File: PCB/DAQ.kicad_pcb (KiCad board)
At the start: 2 copper layers, 164 x 140 mm, 58 parts, among them IC1 MAX743CWE+, J1 Arduino_Mega_Header, J10 Conn_01x01, J11 Conn_01x01, J12 Conn_01x01, J2 Conn_01x07, J3 Conn_01x08, J4 Conn_01x08, J5 Conn_02x18_Counter_Clockwise, J6 Conn_01x10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

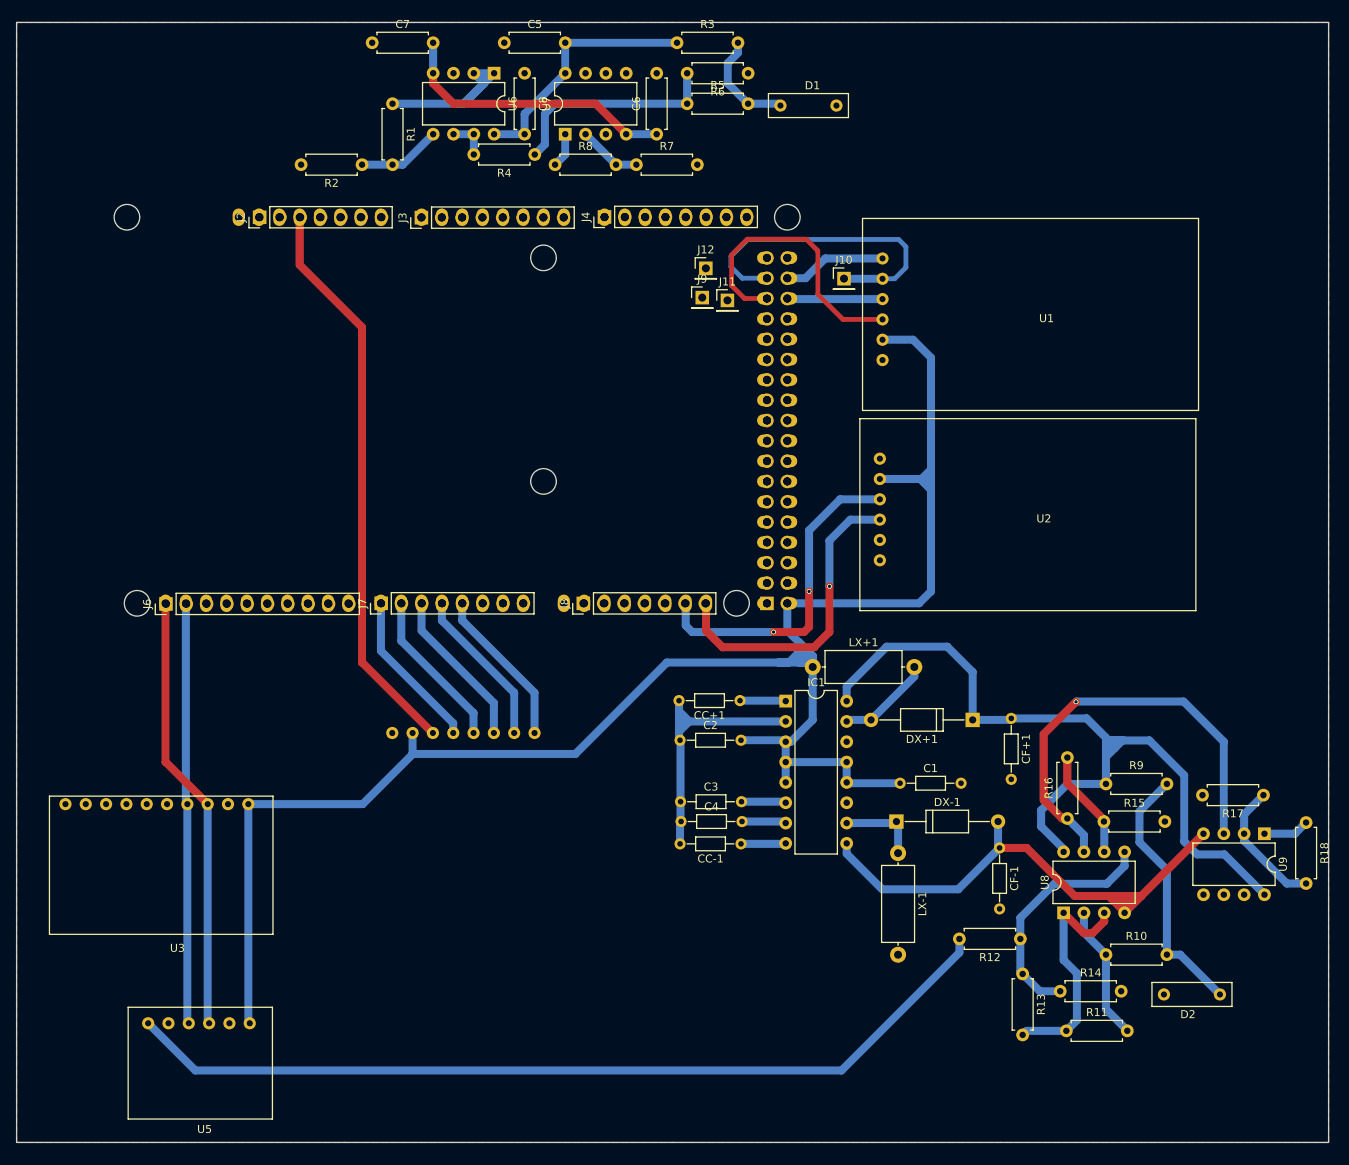
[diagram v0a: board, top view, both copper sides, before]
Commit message: PCB Upgraded and screens of the DAC analog
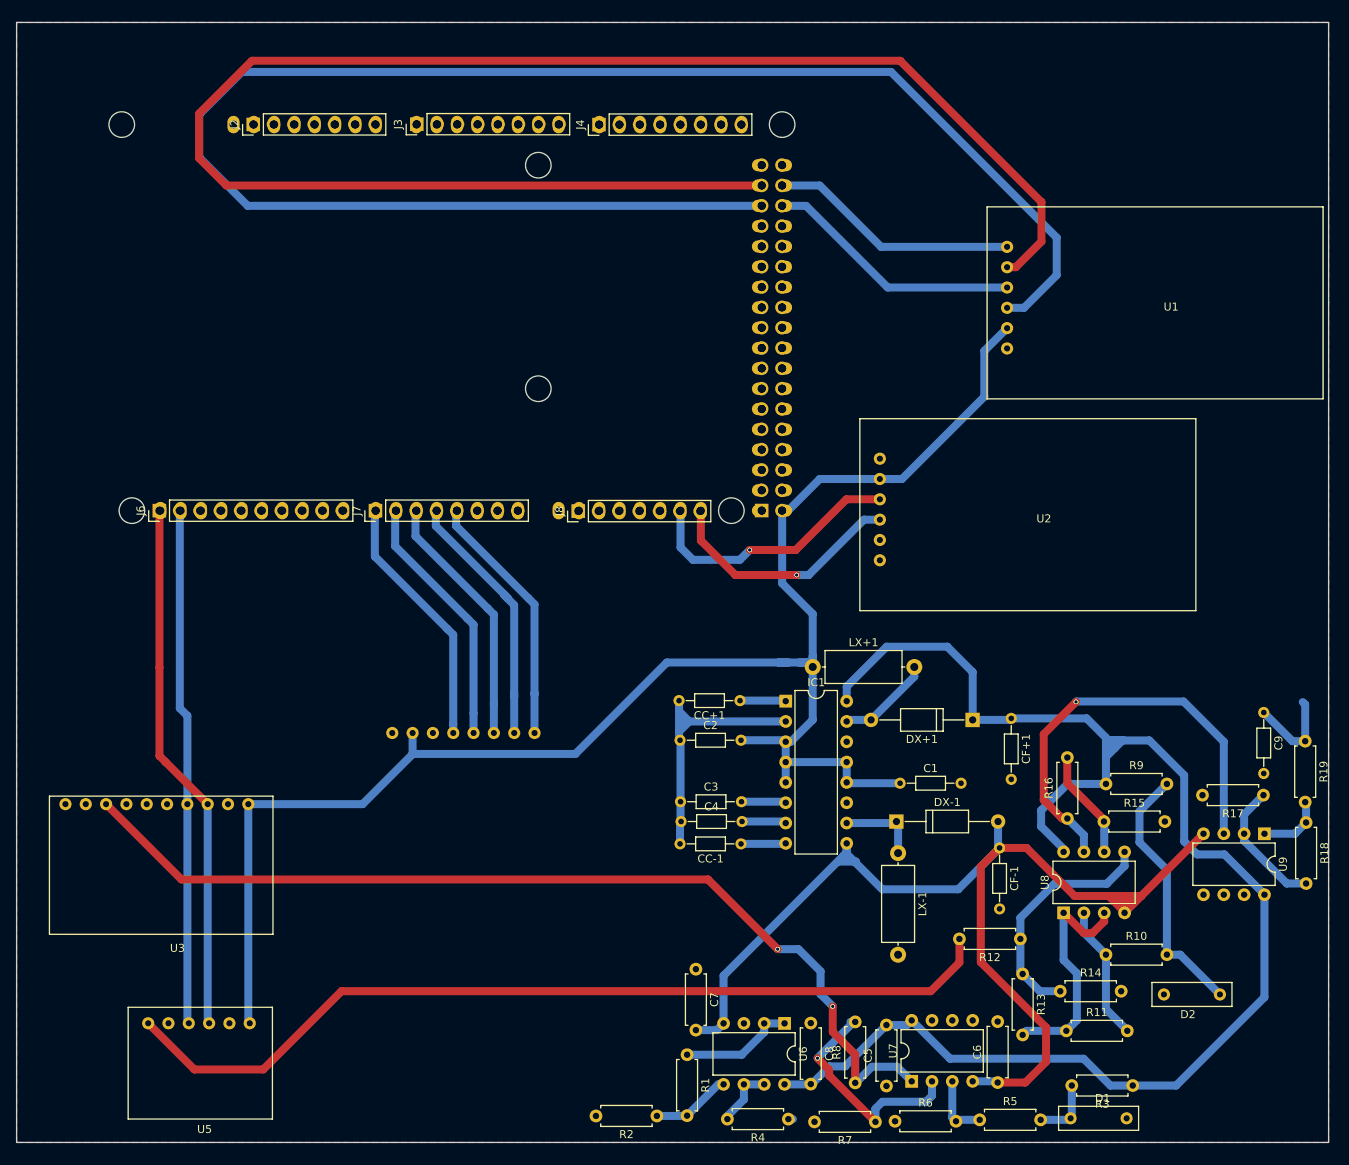
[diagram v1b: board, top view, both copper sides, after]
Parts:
- removed J10, J11, J12, J9: Conn_01x01, Pin_Headers:Pin_Header_Straight_1x01_Pitch2.54mm
- added C9: 100nF, Resistors_THT:R_Axial_DIN0204_L3.6mm_D1.6mm_P7.62mm_Horizontal, F.Cu at (173.4, 106.3)
- added R19: 270k, Resistors_THT:R_Axial_DIN0207_L6.3mm_D2.5mm_P7.62mm_Horizontal, F.Cu at (178.6, 109.8)
- R7: value 47 -> 47k
- moved R3 142.3 mm to (157.0, 152.9), turned to 180 degrees
- moved C5 138.9 mm to (126.2, 152.9), turned to 90 degrees
- moved R6 132.3 mm to (127.3, 157.4), turned to 0 degrees
- moved R5 132.2 mm to (137.9, 157.2)
- moved D1 131.7 mm to (147.8, 155.5)
- moved U7 126.1 mm to (129.4, 152.4)
- moved C6 126.0 mm to (140.1, 152.5)
- moved R4 124.7 mm to (114.0, 157.1)
- moved R2 124.5 mm to (97.5, 156.7)
- moved R1 124.4 mm to (101.3, 149.0)
- moved U6 124.2 mm to (113.5, 145.1)
- moved C8 124.0 mm to (116.8, 145.1)
- moved R7 123.3 mm to (124.9, 157.4), turned to 180 degrees
- moved C7 122.7 mm to (102.4, 138.3), turned to 270 degrees
- moved R8 120.7 mm to (122.3, 152.6), turned to 90 degrees
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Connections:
- net /Vo renamed /VoDAC1
- C5 pad 2: /15V -> /+15V
- C8 pad 2: /15V -> /+15V
- R3 pad 1: /15V -> /+15V
- R8 pad 1: Net-(R8-Pad1) -> /VinADC
- U3 pad 8: Net-(U3-Pad8) -> /VinADC
- U6 pad 8: /15V -> /+15V
- U7 pad 1: Net-(R8-Pad1) -> /VinADC
- U7 pad 8: /15V -> /+15V
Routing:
- net Net-(J5-Pad31): track 2.80 -> 200.9 mm
- net Net-(J5-Pad33): track 3.10 -> 197.6 mm
- net /VinADC: track 0.00 -> 122.4 mm, vias 0 -> 2
- net /+15V: track 107.2 -> 191.2 mm
- net /3.3V: track 71.4 -> 0.05 mm
- net /-15V: track 113.5 -> 155.4 mm
- net /5V: track 253.0 -> 214.8 mm
- net /PIN52: track 43.2 -> 10.3 mm
- net /15V: track 31.3 -> 0.00 mm
- net /PIN50: track 33.2 -> 7.89 mm
- net Net-(R7-Pad1): track 7.93 -> 29.3 mm, vias 0 -> 1
- net /PIN51: track 12.0 -> 32.4 mm
- net /PIN53: track 7.16 -> 26.6 mm
- net Net-(R4-Pad1): track 27.7 -> 9.57 mm
- net /PIN4: track 20.0 -> 33.3 mm
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
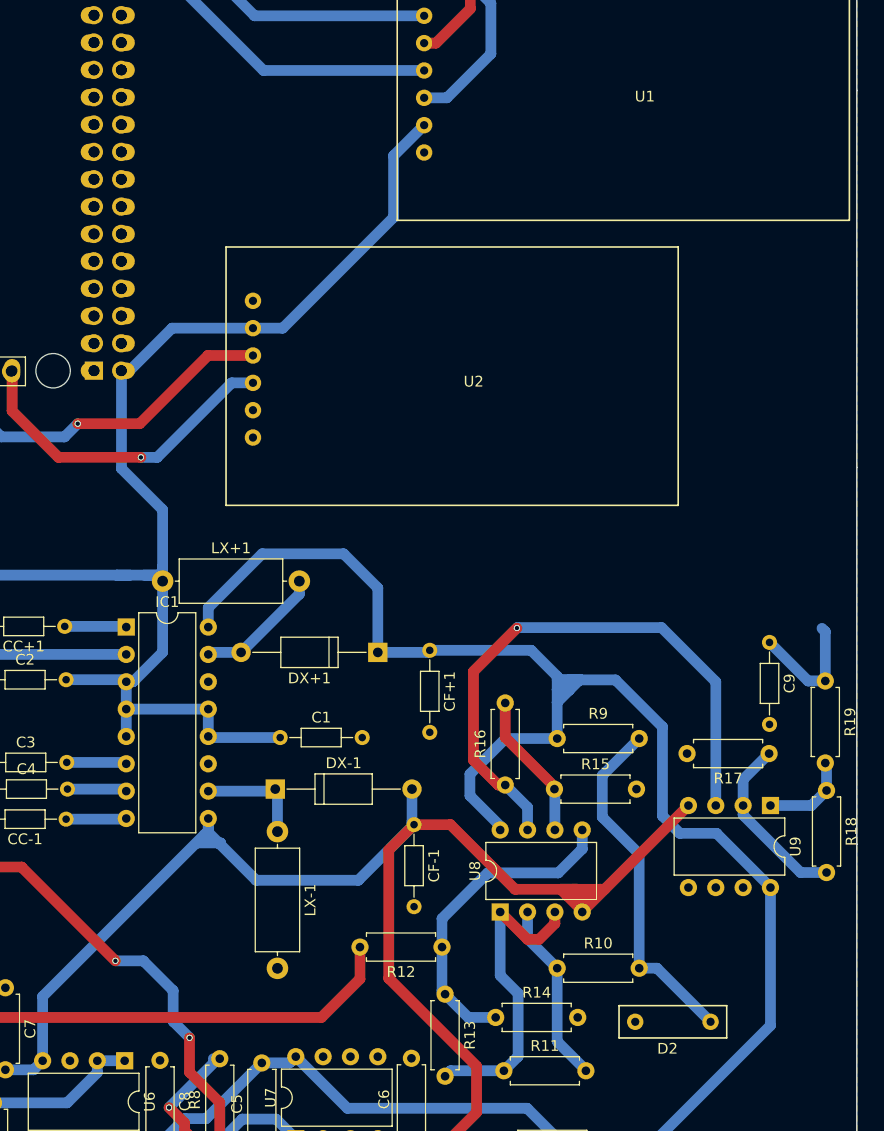
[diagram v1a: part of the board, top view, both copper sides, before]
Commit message: Code modulation and PCB improvements. Multiplexer added
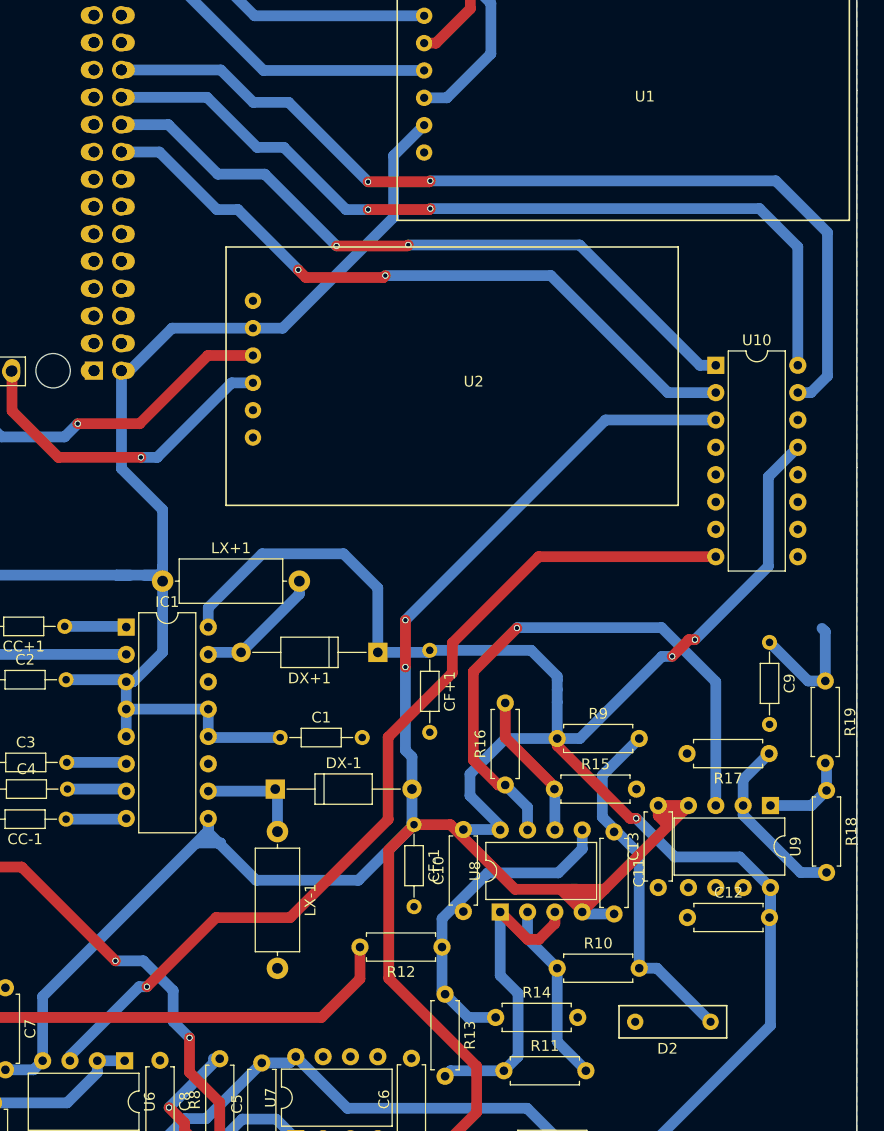
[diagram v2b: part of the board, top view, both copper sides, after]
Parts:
- added C10: 100nF, Resistors_THT:R_Axial_DIN0207_L6.3mm_D2.5mm_P7.62mm_Horizontal, F.Cu at (145.0, 131.3)
- added C11: 100nF, Resistors_THT:R_Axial_DIN0207_L6.3mm_D2.5mm_P7.62mm_Horizontal, F.Cu at (159.0, 123.9)
- added C12: 100nF, Resistors_THT:R_Axial_DIN0207_L6.3mm_D2.5mm_P7.62mm_Horizontal, F.Cu at (165.8, 131.8)
- added C13: 100nF, Resistors_THT:R_Axial_DIN0207_L6.3mm_D2.5mm_P7.62mm_Horizontal, F.Cu at (163.1, 129.0)
- added U10: ADG408, Housings_DIP:DIP-16_W7.62mm, F.Cu at (168.4, 80.5)
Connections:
- J1 pad 49: Net-(J1-Pad49) -> /m_A2
- J1 pad 50: Net-(J1-Pad50) -> /m_A1
- J1 pad 51: Net-(J1-Pad51) -> /m_A0
- J1 pad 52: Net-(J1-Pad52) -> /EN
- J1 pad 53: /PIN35 -> Net-(J1-Pad53)
- J1 pad 54: /PIN33 -> Net-(J1-Pad54)
- J1 pad 55: /PIN31 -> Net-(J1-Pad55)
- J5 pad 12: /PIN31 -> Net-(J5-Pad12)
- J5 pad 14: /PIN33 -> Net-(J5-Pad14)
- J5 pad 16: /PIN35 -> Net-(J5-Pad16)
- J5 pad 18: Net-(J5-Pad18) -> /EN
- J5 pad 20: Net-(J5-Pad20) -> /m_A0
- J5 pad 22: Net-(J5-Pad22) -> /m_A1
- J5 pad 24: Net-(J5-Pad24) -> /m_A2
- U6 pad 3: Net-(U6-Pad3) -> /D
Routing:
- net /PIN52: track 10.3 -> 151.8 mm
- net Net-(J5-Pad31): track 200.9 -> 64.3 mm
- net /PIN50: track 7.89 -> 144.5 mm
- net Net-(J5-Pad33): track 197.6 -> 66.9 mm
- net /m_A2: track 0.00 -> 88.6 mm, vias 0 -> 2
- net /D: track 0.00 -> 85.8 mm, vias 0 -> 1
- net /m_A1: track 0.00 -> 79.7 mm, vias 0 -> 2
- net /-15V: track 155.4 -> 226.3 mm, vias 0 -> 2
- net /EN: track 0.00 -> 64.6 mm, vias 0 -> 2
- net /m_A0: track 0.00 -> 64.5 mm, vias 0 -> 2
- net /+15V: track 191.2 -> 221.0 mm, vias 0 -> 3
- net /PIN53: track 26.6 -> 15.8 mm

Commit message: Start of LaTeX proyect and few improvements
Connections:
- C10 pad 1: Net-(C10-Pad1) -> /GND
- C11 pad 1: Net-(C11-Pad1) -> /GND
- C12 pad 1: Net-(C12-Pad1) -> /GND
- C13 pad 1: Net-(C13-Pad1) -> /GND
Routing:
- net Net-(J5-Pad31): track 64.3 -> 196.2 mm
- net /PIN50: track 144.5 -> 12.6 mm

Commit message: New version of PCB
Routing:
- net Net-(J5-Pad31): track 196.2 -> 166.9 mm
- net /PIN50: track 12.6 -> 41.9 mm
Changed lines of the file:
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@@
     (links 161)
     (no_connects 12)
-    (area 17.424999 19.924999 181.575001 160.075001)
+    (area 16.283999 19.924999 182.0734 160.81424)
     (thickness 1.6)
-    (drawings 13)
+    (drawings 14)
     (tracks 453)
     (zones 0)
@@
     )
   )
+  (target plus (at 17.49492 20.03556) (size 5) (width 0.15) (layer Edge.Cuts))
   (gr_line (start 58.5 20) (end 17.5 20) (angle 90) (layer Edge.Cuts) (width 0.15))
   (gr_line (start 99.5 20) (end 58.5 20) (angle 90) (layer Edge.Cuts) (width 0.15))
@@
   (segment (start 143.4243 55.67304) (end 147.5099 51.58744) (width 1) (layer B.Cu) (net 42))
   (segment (start 147.5099 51.58744) (end 147.5099 46.88844) (width 1) (layer B.Cu) (net 42))
+  (segment (start 147.5099 46.88844) (end 126.8089 26.18744) (width 1) (layer B.Cu) (net 42))
   (segment (start 82.24 103.92414) (end 82.24 92.741) (width 1) (layer B.Cu) (net 58))
   (segment (start 72.4408 82.9418) (end 72.4408 80.7974) (width 1) (layer B.Cu) (net 58))
@@
   (segment (start 45.6559 26.18744) (end 40.3219 31.52144) (width 1) (layer B.Cu) (net 109))
   (segment (start 126.8089 26.18744) (end 45.6559 26.18744) (width 1) (layer B.Cu) (net 109))
-  (segment (start 147.5099 46.88844) (end 126.8089 26.18744) (width 1) (layer B.Cu) (net 109))
   (segment (start 46.3925 42.92604) (end 110.6545 42.92604) (width 1) (layer B.Cu) (net 109))
   (segment (start 43.7255 40.38604) (end 110.6545 40.38604) (width 1) (layer F.Cu) (net 110))
